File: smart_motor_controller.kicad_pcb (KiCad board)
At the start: 4 copper layers, 75 x 60 mm, 76 parts, among them J10 USB_B_Micro, J101 Breakout, J102 I2C_CONN, J103 CAN_CONN, J104 Debug, J301 M0_CONN, J302 M1_CONN, J303 M2_CONN, J304 M3_CONN, J309 External encoders power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

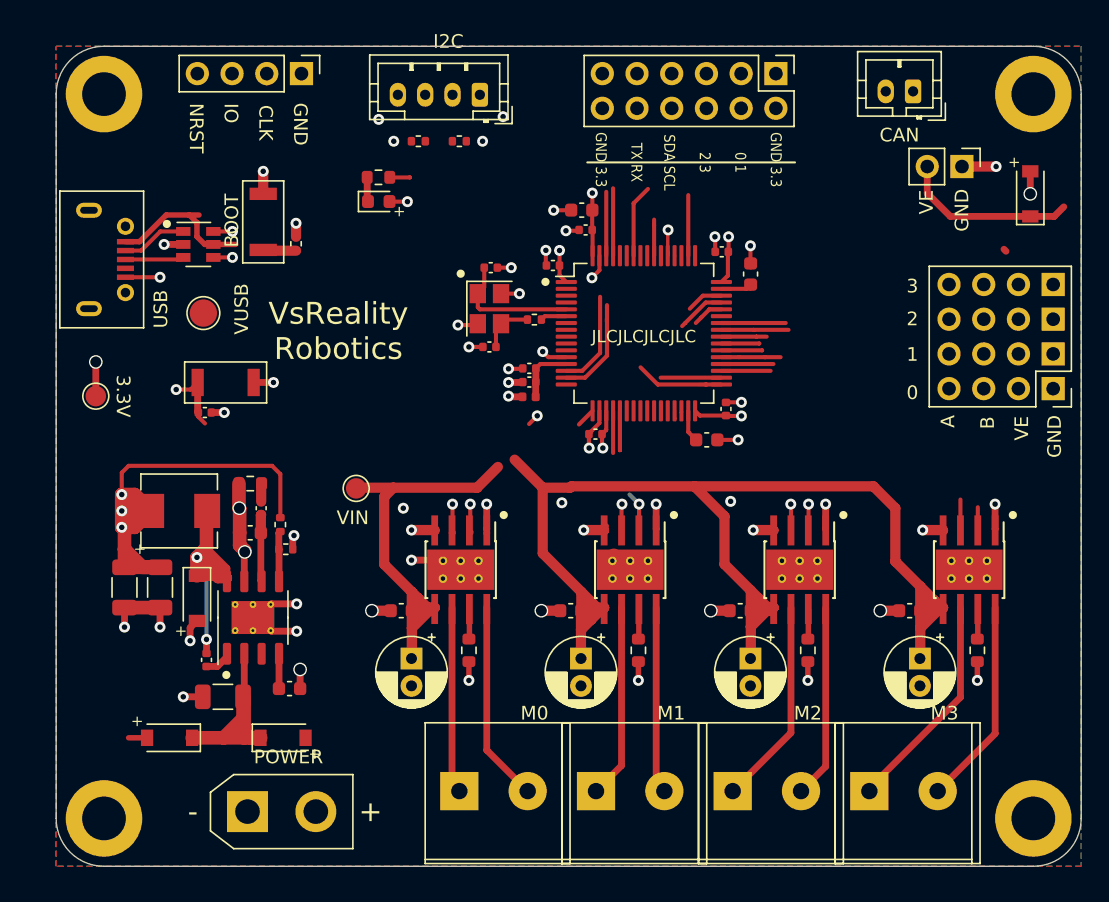
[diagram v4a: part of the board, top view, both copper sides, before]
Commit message: Change components to 0603
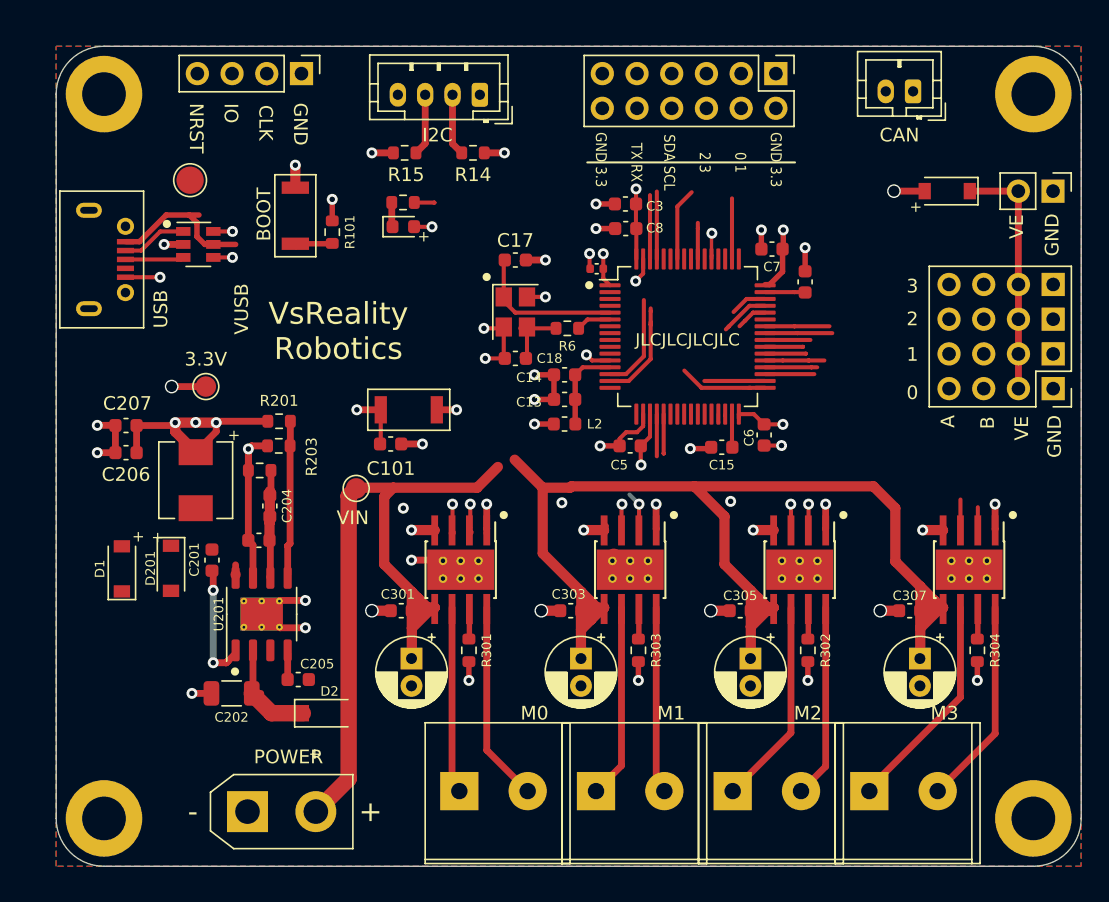
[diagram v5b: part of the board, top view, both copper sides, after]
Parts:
- C101, C13, C14, C17, C18, C201, C204, C5, C6, C7, C8: footprint Capacitor_SMD:C_0402_1005Metric -> Capacitor_SMD:C_0603_1608Metric
- C206, C207: footprint Capacitor_SMD:C_1206_3216Metric -> Capacitor_SMD:C_0603_1608Metric
- L2: footprint Inductor_SMD:L_0402_1005Metric -> Inductor_SMD:L_0603_1608Metric
- R101, R14, R15, R201, R203, R6: footprint Resistor_SMD:R_0402_1005Metric -> Resistor_SMD:R_0603_1608Metric
- moved C101 13.8 mm to (147.5, 84.6)
- moved SW103 13.5 mm to (148.8, 82.1)
- moved D1 12.8 mm to (127.8, 93.7), turned to 90 degrees
- moved C207 11.9 mm to (128.1, 83.2), turned to 180 degrees
- moved C206 10.2 mm to (128.1, 85.2), turned to 180 degrees
- moved TP2 9.77 mm to (132.8, 65.3)
- moved 3.3V201 8.08 mm to (133.9, 80.4), turned to 0 degrees
- moved R203 7.58 mm to (139.3, 84.7), turned to 180 degrees
- moved R201 7.56 mm to (139.3, 82.9), turned to 0 degrees
- moved C201 7.31 mm to (134.4, 93.1)
- moved J309 6.90 mm to (195.9, 66.1)
- moved D301 6.08 mm to (188.2, 66.1), turned to 180 degrees
- moved C16 4.03 mm to (177.8, 72.7)
- moved C7 3.68 mm to (175.4, 70.3)
- moved D2 3.58 mm to (142.7, 104.3)
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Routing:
- net VMOTORS: track 124.3 -> 149.2 mm
- net Net-(D201-K): track 22.9 -> 0.76 mm, vias 2 -> 0
- net +3V3: track 68.7 -> 55.0 mm, vias 19 -> 18
- net GND: track 76.9 -> 85.4 mm, vias 49 -> 43
- net BACK_IN: track 16.0 -> 8.07 mm
- net Net-(U201-VSENSE): track 3.47 -> 11.3 mm
- net Net-(U201-BOOT): track 1.79 -> 8.94 mm, vias 0 -> 2
- net V_ENCODER: track 13.2 -> 18.0 mm
- net I2C1_SCL: track 4.94 -> 9.46 mm
- net I2C1_SDA: track 4.68 -> 9.20 mm
- net Net-(C204-Pad2): track 1.33 -> 3.19 mm
- net +3.3VA: track 4.56 -> 6.38 mm
- net HSE_IN: track 9.63 -> 11.1 mm
- net GPIO1: track 1.50 -> 0.08 mm
- net +5V: track 12.4 -> 11.1 mm
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
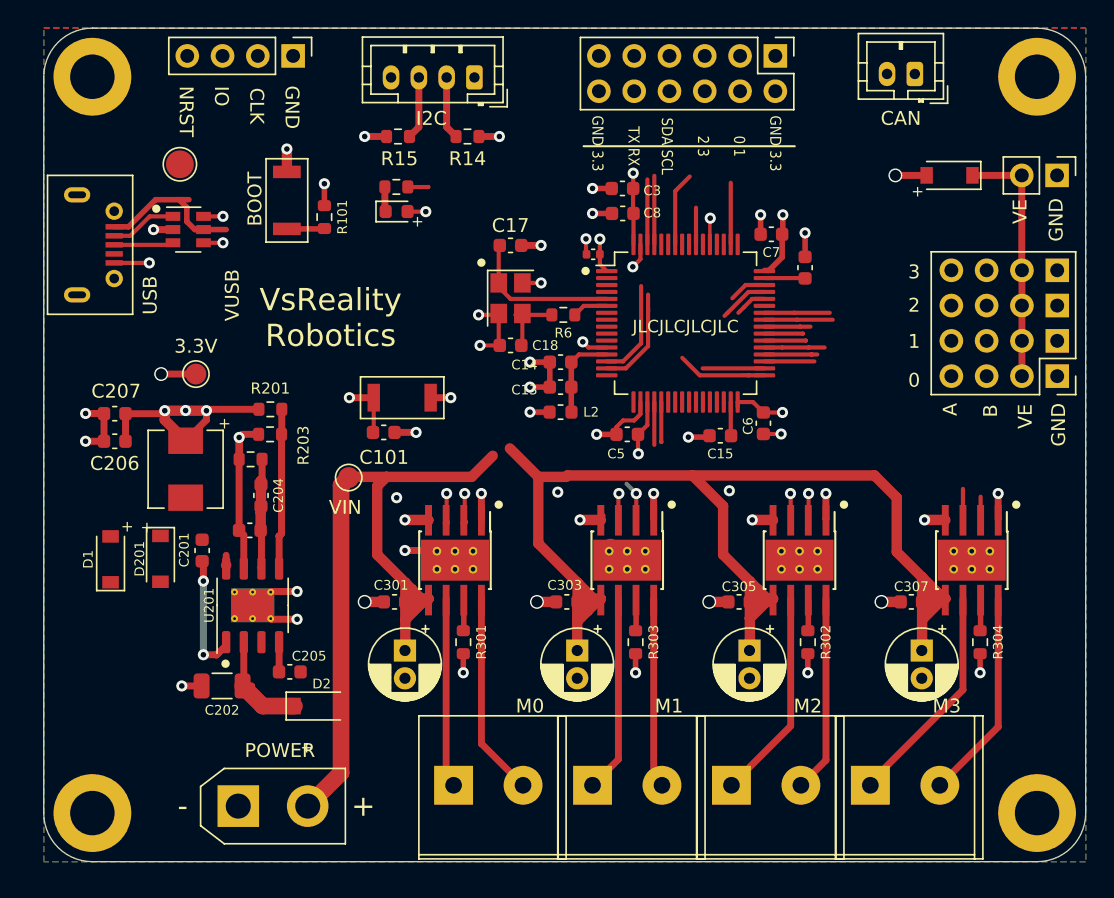
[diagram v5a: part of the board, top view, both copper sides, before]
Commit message: Reorganized motor drivers
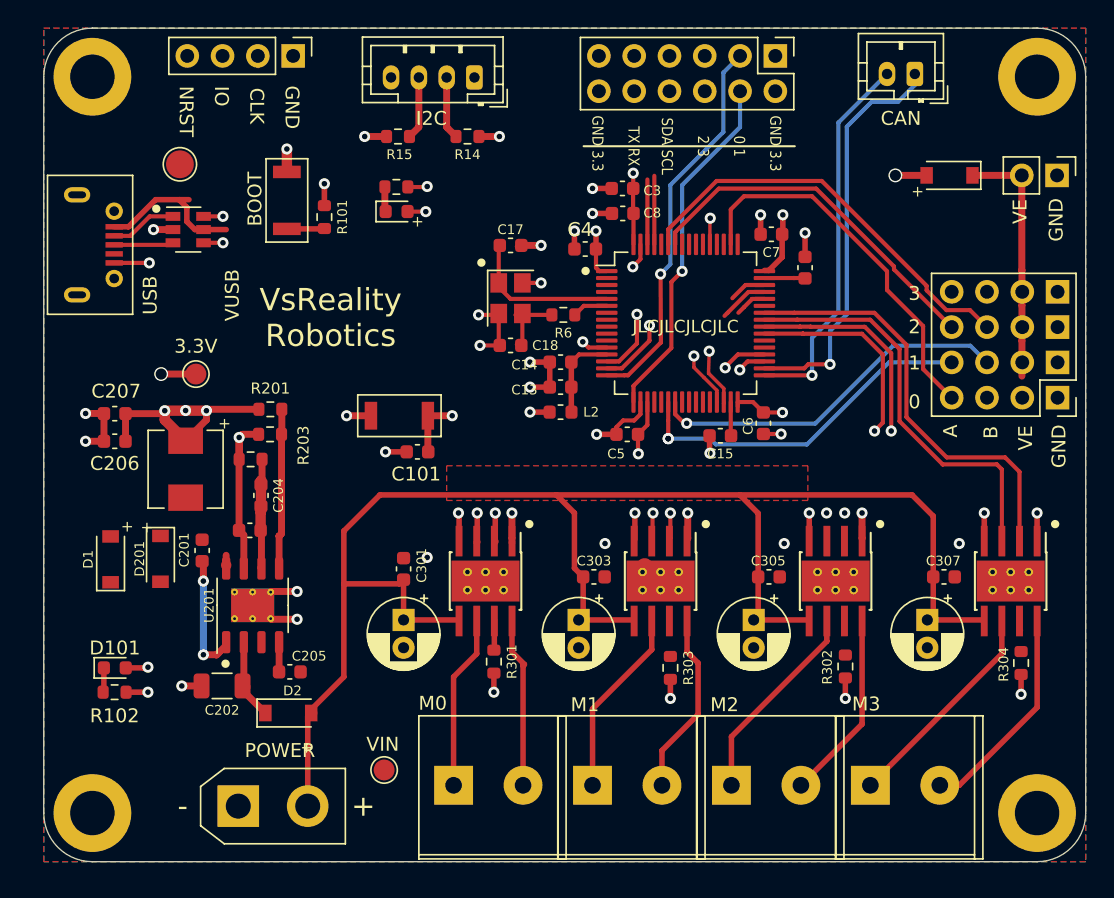
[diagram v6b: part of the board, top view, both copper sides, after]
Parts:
- added D101: RED, LED_SMD:LED_0603_1608Metric, F.Cu at (128.1, 101.5)
- added R102: 120, Resistor_SMD:R_0603_1608Metric, F.Cu at (128.1, 103.3)
- C4: footprint Capacitor_SMD:C_0402_1005Metric -> Capacitor_SMD:C_0603_1608Metric
- moved TP1 21.2 mm to (147.5, 108.9)
- moved R304 3.31 mm to (193.3, 101.2)
- moved R302 3.22 mm to (180.7, 101.5)
- moved U304 3.18 mm to (192.6, 95.3)
- moved R303 3.11 mm to (168.1, 101.5)
- moved U302 3.00 mm to (180.0, 95.3)
- moved C307 2.96 mm to (187.8, 95.0), turned to 180 degrees
- moved U303 2.83 mm to (167.4, 95.3)
- moved C305 2.80 mm to (175.2, 95.0), turned to 180 degrees
- moved C101 2.80 mm to (149.9, 86.0), turned to 180 degrees
- moved U301 2.66 mm to (154.8, 95.3)
- moved C303 2.65 mm to (162.6, 95.0), turned to 180 degrees
- moved R301 2.61 mm to (155.4, 101.1)
- moved C301 2.46 mm to (148.9, 94.4), turned to -90 degrees
- moved C308 2.24 mm to (186.6, 98.1)
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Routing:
- net VMOTORS: track 149.2 -> 116.1 mm
- net ENCODER_2_B: track 0.00 -> 30.0 mm
- net GPIO0: track 0.00 -> 28.0 mm, vias 0 -> 1
- net ENCODER_1_B: track 0.00 -> 26.5 mm, vias 0 -> 1
- net ENCODER_1_A: track 0.00 -> 25.8 mm, vias 0 -> 2
- net GPIO1: track 0.08 -> 25.6 mm, vias 0 -> 1
- net CAN2_TX: track 4.45 -> 29.4 mm, vias 0 -> 1
- net M3_OUT2: track 6.31 -> 31.1 mm
- net ENCODER_0_A: track 4.44 -> 27.4 mm
- net M3_OUT1: track 7.08 -> 29.8 mm
- net ENCODER_2_A: track 5.32 -> 26.3 mm
- net CAN2_RX: track 6.91 -> 27.4 mm, vias 0 -> 1
- net M1_OUT2: track 5.15 -> 15.6 mm, vias 1 -> 2
- net M1_OUT1: track 4.62 -> 14.9 mm, vias 1 -> 2
- net GND: track 85.4 -> 79.9 mm, vias 43 -> 41
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- added copper zone on F.Cu, net VMOTORS

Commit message: Complete layout
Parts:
- moved C101 2.40 mm to (149.8, 83.6)
- moved SW103 2.40 mm to (148.5, 81.0)
- moved C13 2.26 mm to (160.5, 79.1)
- moved C14 2.26 mm to (160.5, 77.3)
- moved C15 2.26 mm to (172.0, 82.6)
- moved C18 2.26 mm to (156.9, 76.1)
- moved C3 2.26 mm to (165.0, 64.8)
- moved C4 2.26 mm to (162.3, 69.2)
- moved C7 2.26 mm to (175.7, 68.1)
- moved C8 2.26 mm to (165.0, 66.6)
- moved C17 2.26 mm to (156.9, 68.9)
- moved C5 2.26 mm to (165.3, 82.5)
- moved HSE1 2.26 mm to (156.9, 72.7)
- moved L2 2.26 mm to (160.5, 80.9)
- moved U2 2.26 mm to (169.5, 74.5)
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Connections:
- J101 pad 10: USART3_RX -> I2C1_SCL
- J101 pad 3: GPIO0 -> USART3_TX
- J101 pad 4: GPIO1 -> USART3_RX
- J101 pad 7: I2C2_SDA -> GPIO0
- J101 pad 8: I2C2_SCL -> GPIO1
- J101 pad 9: USART3_TX -> I2C1_SDA
- J102 pad 2: I2C1_SCL -> I2C2_SCL
- J102 pad 3: I2C1_SDA -> I2C2_SDA
- R14 pad 2: I2C1_SCL -> I2C2_SCL
- R15 pad 2: I2C1_SDA -> I2C2_SDA
- U2 pad 14: ENCODER_3_A -> ENCODER_1_A
- U2 pad 15: ENCODER_3_B -> ENCODER_1_B
- U2 pad 16: GPIO0 -> LED
- U2 pad 17: GPIO1 -> unconnected-(U2-PA3-Pad17)
- U2 pad 20: GPIO2 -> unconnected-(U2-PA4-Pad20)
- U2 pad 21: GPIO3 -> unconnected-(U2-PA5-Pad21)
- U2 pad 22: ENCODER_1_A -> ENCODER_0_A
- U2 pad 23: ENCODER_1_B -> ENCODER_0_B
- U2 pad 50: ENCODER_0_A -> ENCODER_3_A
- U2 pad 53: LED -> GPIO3
- U2 pad 54: unconnected-(U2-PD2-Pad54) -> GPIO2
- U2 pad 55: ENCODER_0_B -> ENCODER_3_B
- U2 pad 56: unconnected-(U2-PB4-Pad56) -> GPIO1
- U2 pad 57: unconnected-(U2-PB5-Pad57) -> GPIO0
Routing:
- net NRST: track 4.36 -> 56.9 mm, vias 1 -> 2
- net USB_D-: track 3.69 -> 49.8 mm, vias 1 -> 2
- net SWDIO: track 2.81 -> 47.2 mm, vias 0 -> 1
- net SWCLK: track 0.34 -> 43.7 mm, vias 0 -> 1
- net USB_D+: track 4.99 -> 46.7 mm, vias 1 -> 2
- net I2C2_SDA: track 4.34 -> 41.2 mm, vias 1 -> 2
- net I2C2_SCL: track 4.65 -> 38.6 mm, vias 1 -> 2
- net BOOT0: track 2.80 -> 36.2 mm, vias 0 -> 2
- net M0_OUT1: track 4.25 -> 34.0 mm
- net +5V: track 11.1 -> 40.2 mm
- net M0_OUT2: track 5.61 -> 34.4 mm
- net ENCODER_0_B: track 0.00 -> 28.1 mm, vias 0 -> 1
- net M2_OUT2: track 1.83 -> 27.9 mm, vias 1 -> 2
- net M2_OUT1: track 1.84 -> 27.0 mm, vias 1 -> 2
- net LED: track 3.48 -> 24.9 mm
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- added copper zone on F.Cu, net +3V3
- added copper zone on F.Cu, net Net-(D201-K)
- added copper zone on F.Cu, net Net-(J301-Pin_1)
- added copper zone on F.Cu, net Net-(J301-Pin_2)
- added copper zone on F.Cu, net Net-(J302-Pin_1)
- added copper zone on F.Cu, net Net-(J302-Pin_2)
- added copper zone on F.Cu, net Net-(J303-Pin_1)
- added copper zone on F.Cu, net Net-(J303-Pin_2)
- added copper zone on F.Cu, net Net-(J304-Pin_1)
- added copper zone on F.Cu, net Net-(J304-Pin_2)
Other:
- board text added: "1 0"
- board text added: "3 2"
- board text added: "3.3 GND"
- board text added: "4 5"
- board text added: "5 4"
- board text added: "6 7"
- board text added: "7 6"
- board text added: "ENCODERS"
- board text added: "M4"

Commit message: Updated gedber files
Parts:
- removed J103: CAN_CONN, Connector_JST:JST_PH_B2B-PH-K_1x02_P2.00mm_Vertical
- added R103: 15, Resistor_SMD:R_0603_1608Metric, F.Cu at (142.4, 73.8)
- added R104: 15, Resistor_SMD:R_0603_1608Metric, F.Cu at (142.4, 75.3)
- J101: value Breakout -> Conn_02x07_Odd_Even; footprint Connector_PinHeader_2.54mm:PinHeader_2x06_P2.54mm_Vertical -> Connector_PinHeader_2.54mm:PinHeader_2x07_P2.54mm_Vertical
- R101: value 10k -> 10K
- moved J101 8.77 mm to (184.4, 57.4)
- moved R14 4.00 mm to (157.5, 63.2)
- moved J102 3.90 mm to (157.9, 59.1)
- moved R15 3.85 mm to (152.3, 63.2)
- moved TP1 1.58 mm to (147.8, 107.3)
- moved C16 1.52 mm to (177.5, 71.9), turned to -90 degrees
- moved C7 1.47 mm to (176.8, 69.1), turned to 0 degrees
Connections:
- J10 pad 6: unconnected-(J10-Shield-Pad6) -> GND
- J101 pad 10: I2C1_SCL -> GPIO1
- J101 pad 11: GND -> I2C1_SDA
- J101 pad 12: +3V3 -> I2C1_SCL
- J101 pad 3: USART3_TX -> CAN2_TX
- J101 pad 4: USART3_RX -> CAN2_RX
- J101 pad 5: GPIO2 -> USART3_TX
- J101 pad 6: GPIO3 -> USART3_RX
- J101 pad 7: GPIO0 -> GPIO2
- J101 pad 8: GPIO1 -> GPIO3
- J101 pad 9: I2C1_SDA -> GPIO0
- U3 pad 4: USB_D+ -> Net-(R104-Pad2)
- U3 pad 6: USB_D- -> Net-(R103-Pad1)
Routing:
- net USB_D-: track 49.8 -> 37.6 mm
- net USB_D+: track 46.7 -> 37.4 mm
- net GND: track 83.9 -> 93.1 mm, vias 63 -> 68
- net Net-(R103-Pad1): track 0.00 -> 7.82 mm
- net Net-(R104-Pad2): track 0.00 -> 7.67 mm
- net USART3_RX: track 9.45 -> 14.4 mm
- net USART3_TX: track 12.7 -> 17.6 mm
- net I2C2_SDA: track 41.2 -> 36.7 mm
- net GPIO3: track 9.42 -> 13.4 mm
- net I2C2_SCL: track 38.6 -> 34.7 mm
- net GPIO2: track 12.4 -> 15.4 mm
- net GPIO1: track 9.49 -> 11.4 mm
- net CAN2_RX: track 35.5 -> 33.6 mm
- net NRST: track 56.9 -> 58.4 mm
- net Net-(C204-Pad2): track 3.19 -> 1.86 mm
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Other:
- board text added: "3.3V GND"
- board text added: "6.5-28V"
- board text added: "8 9"
- board text added: "9 8"
- board text added: "GND 3.3V"
- board text added: "VDC"
- board text removed: "3.3 GND"
- board text removed: "CAN"
- board text removed: "GND 3.3"
- board text removed: "RX"
- board text removed: "SDA SCL"
- board text removed: "TX"
- board text removed: "TX RX"
- board text removed: "USART"
